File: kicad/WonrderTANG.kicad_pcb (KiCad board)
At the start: 2 copper layers, 101.6 x 90.2 mm, 31 parts, among them CON1 MSX-CONNECTOR, J1 Conn_02x01, J2 AudioJack3, J3 Conn_02x01, Q1 2N3904, U1 SN74LVC245AN, U2 SN74LVC245AN, U3 SN74LVC245AN, U4 SN74LVC245AN, U5 Tang_Nano_20k, U6 SN74LVC245AN

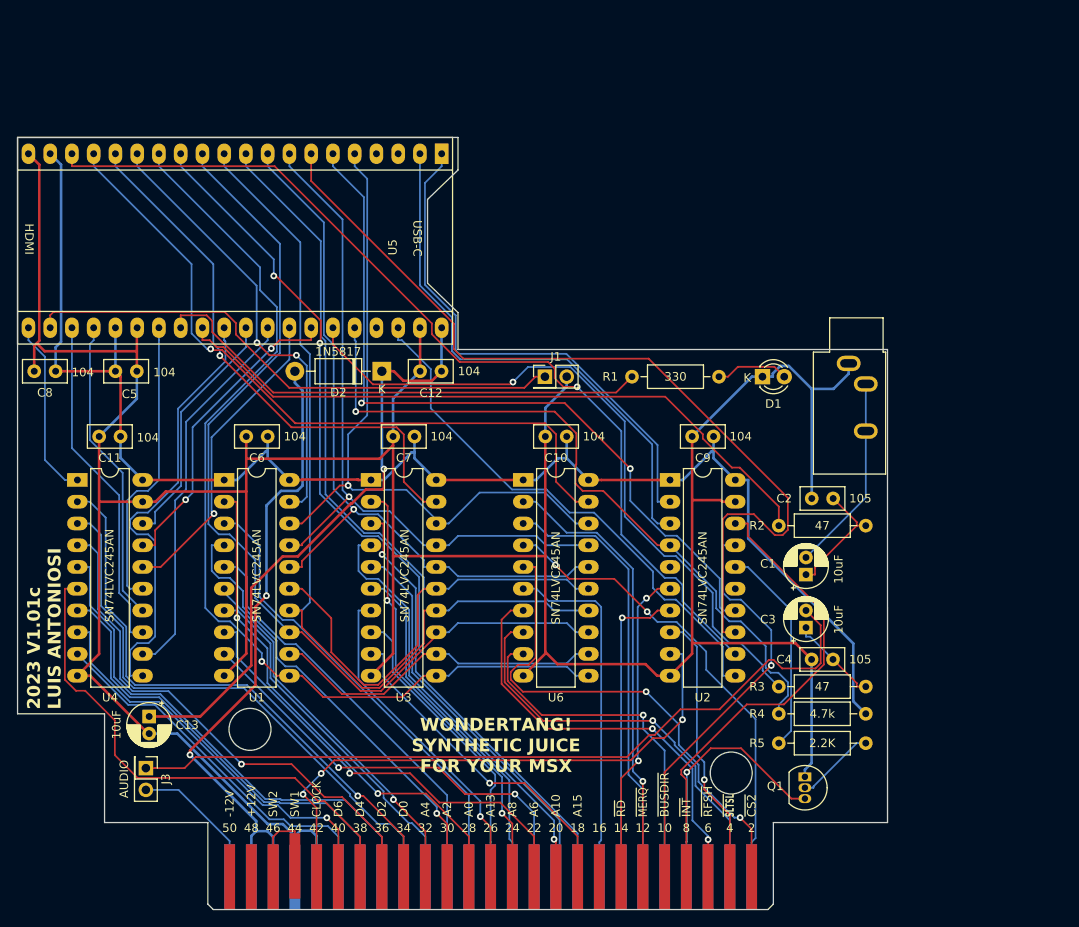
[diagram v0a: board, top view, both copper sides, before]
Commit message: New PCB Version 1.0.2d
A new firmware inverting the INT outpult needs to be submitted.
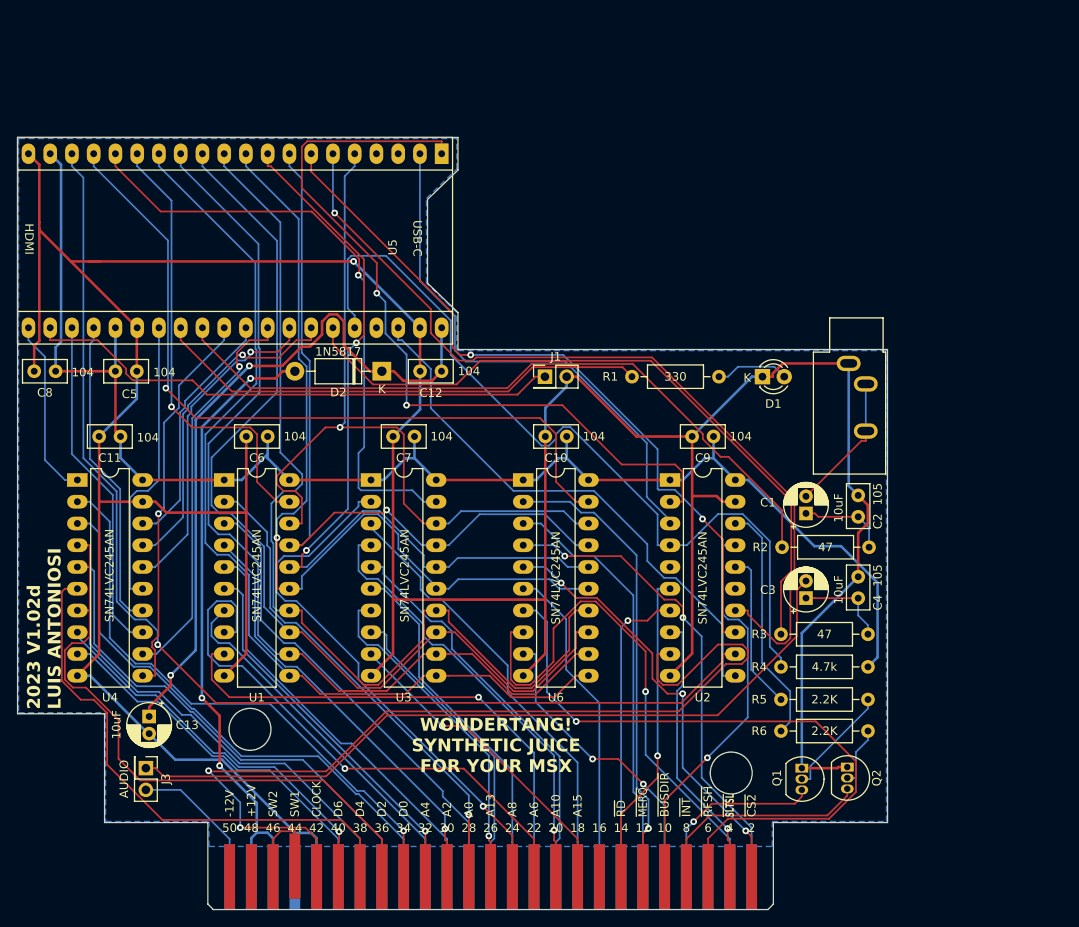
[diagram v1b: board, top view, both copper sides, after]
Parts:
- added Q2: 2N3904, Package_TO_SOT_THT:TO-92_Inline, F.Cu at (153.4, 126.9)
- added R6: 2.2K, Resistor_THT:R_Axial_DIN0207_L6.3mm_D2.5mm_P10.16mm_Horizontal, F.Cu at (145.7, 122.7)
- moved C4 7.73 mm to (154.7, 107.1), turned to 90 degrees
- moved C1 7.14 mm to (148.6, 97.2)
- moved R3 6.12 mm to (145.7, 111.4)
- moved R4 5.49 mm to (155.8, 115.2)
- moved R5 5.11 mm to (145.7, 119.0)
- moved C2 3.62 mm to (154.7, 97.6), turned to 90 degrees
- moved C3 3.45 mm to (148.6, 107.1)
- moved R2 2.55 mm to (145.8, 101.2)
- moved Q1 1.08 mm to (148.1, 127.0)
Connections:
- U2 pad 18: INT -> /INT_SW
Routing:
- net GND: track 406.2 -> 451.9 mm, vias 0 -> 1
- net CLOCK: track 67.5 -> 109.0 mm, vias 3 -> 2
- net INT_33: track 61.5 -> 93.7 mm, vias 0 -> 2
- net INT: track 56.1 -> 26.1 mm
- net RFSH: track 50.3 -> 78.5 mm, vias 2 -> 1
- net /INT_SW: track 0.00 -> 28.2 mm
- net SLTSL_33: track 112.1 -> 135.4 mm
- net WR_33: track 103.4 -> 85.4 mm, vias 0 -> 2
- net CS12: track 48.8 -> 62.1 mm
- net RD_33: track 88.6 -> 101.4 mm, vias 2 -> 1
- net WAIT_33: track 83.7 -> 96.4 mm, vias 1 -> 0
- net A6: track 52.7 -> 65.1 mm
- net MP2_33: track 88.0 -> 99.6 mm, vias 1 -> 2
- net A8: track 51.6 -> 63.1 mm, vias 2 -> 1
- net +5V: track 70.5 -> 82.0 mm, vias 1 -> 2
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- added copper zone on B.Cu, net GND
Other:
- board text added: "2023 V1.02d LUIS ANTONIOSI"
- board text removed: "2023 V1.01c LUIS ANTONIOSI"

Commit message: version 2.0b
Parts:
- removed C3: 10uF, Capacitor_THT:CP_Radial_D5.0mm_P2.00mm
- removed C4: 105, Capacitor_THT:C_Disc_D5.0mm_W2.5mm_P2.50mm
- removed J1: Conn_02x01, Connector_PinHeader_2.54mm:PinHeader_2x01_P2.54mm_Vertical
- removed R2, R3: 47, Resistor_THT:R_Axial_DIN0207_L6.3mm_D2.5mm_P10.16mm_Horizontal
- C1: value 10uF -> 4.7u; footprint Capacitor_THT:CP_Radial_D5.0mm_P2.00mm -> Capacitor_THT:CP_Radial_D5.0mm_P2.50mm
- C2: value 105 -> 4.7u; footprint Capacitor_THT:C_Disc_D5.0mm_W2.5mm_P2.50mm -> Capacitor_THT:CP_Radial_D5.0mm_P2.50mm
- CON1: footprint Mis_huellas:CARTRIDGE_MSX -> Tang20K:CARTRIDGE_MSX_NOCUT
- D1: value LED -> uSD
- J2: footprint Connector_Audio:Jack_3.5mm_CUI_SJ1-3533NG_Horizontal -> Tang20K:SJ1-3523N
- J3: value Conn_02x01 -> AUDIO
- Q1, Q2: footprint Package_TO_SOT_THT:TO-92_Inline -> Package_TO_SOT_THT:TO-92_Inline_Wide
- U5: footprint Mis_huellas:Tang_Nano_20k -> Tang20K:Tang_Nano_20k_Audio
- moved J3 86.4 mm to (107.7, 48.5), turned to 0 degrees
- moved C13 70.5 mm to (116.8, 66.6)
- moved C1 58.2 mm to (92.2, 111.8), turned to 0 degrees
- moved Q1 34.3 mm to (170.8, 101.3)
- moved R4 34.1 mm to (176.3, 87.9)
- moved R5 33.3 mm to (166.1, 92.7)
- moved R6 32.4 mm to (166.1, 97.5)
- moved C9 25.2 mm to (158.8, 74.3)
- moved U6 25.2 mm to (136.6, 79.3)
- moved C11 25.2 mm to (89.5, 74.3)
- moved C6 25.2 mm to (106.7, 74.3)
- moved C7 25.2 mm to (123.9, 74.3)
- moved U1 25.2 mm to (101.6, 79.3)
- moved U3 25.2 mm to (118.8, 79.3)
- moved U4 25.2 mm to (84.5, 79.3)
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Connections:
- C1 pad 1: Net-(C1-Pad1) -> Net-(J3-Pin_1)
- C1 pad 2: Net-(C1-Pad2) -> SOUNDIN
- C2 pad 1: Net-(C1-Pad1) -> Net-(J3-Pin_2)
- C2 pad 2: GND -> Net-(C2-Pad2)
- J2 pad R: Net-(C1-Pad2) -> Net-(C2-Pad2)
- J2 pad T: Net-(C1-Pad2) -> Net-(C2-Pad2)
- J3 pad 2: SOUNDIN -> Net-(J3-Pin_2)
- U5 pad 22: JP -> D6_33
- U5 pad 28: LED -> D2_33
- U5 pad 29: SOUND_33 -> D7_33
- U5 pad 3: unconnected-(U5-75_IOT34A-Pad3) -> LED
- U5 pad 35: AUDIO_33 -> D1_33
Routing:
- net SOUND_33: track 84.4 -> 0.00 mm
- net AUDIO_33: track 81.4 -> 0.00 mm
- net Net-(J3-Pin_2): track 0.00 -> 78.3 mm, vias 0 -> 1
- net JP: track 63.1 -> 0.00 mm
- net +5V: track 82.0 -> 24.9 mm, vias 2 -> 0
- net GND: track 451.9 -> 412.2 mm
- net RFSH: track 78.5 -> 41.1 mm, vias 1 -> 2
- net CLOCK: track 109.0 -> 140.5 mm, vias 2 -> 0
- net SLTSL_33: track 135.4 -> 107.9 mm, vias 1 -> 0
- net CS1: track 56.5 -> 79.9 mm, vias 2 -> 0
- net CS12: track 62.1 -> 40.2 mm
- net A15: track 37.6 -> 58.9 mm, vias 1 -> 0
- net MP4_33: track 116.6 -> 95.8 mm
- net D4_33: track 36.6 -> 57.1 mm
- net LED: track 58.3 -> 38.1 mm
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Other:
- board size 101.6 x 90.2 mm -> 101.6 x 89.5 mm
- board text added: "2024 V2.0b LUIS ANTONIOSI"
- board text added: "SSLT0: uSD Drive + Nextor SSLT1: OPLL + FM ROM SSLT2: 2MB Megaram+SCC SSLT3: 4MB Memory Mapper SMS VDP/PSG (Franky HDMI)"
- board text removed: "2023 V1.02d LUIS ANTONIOSI"

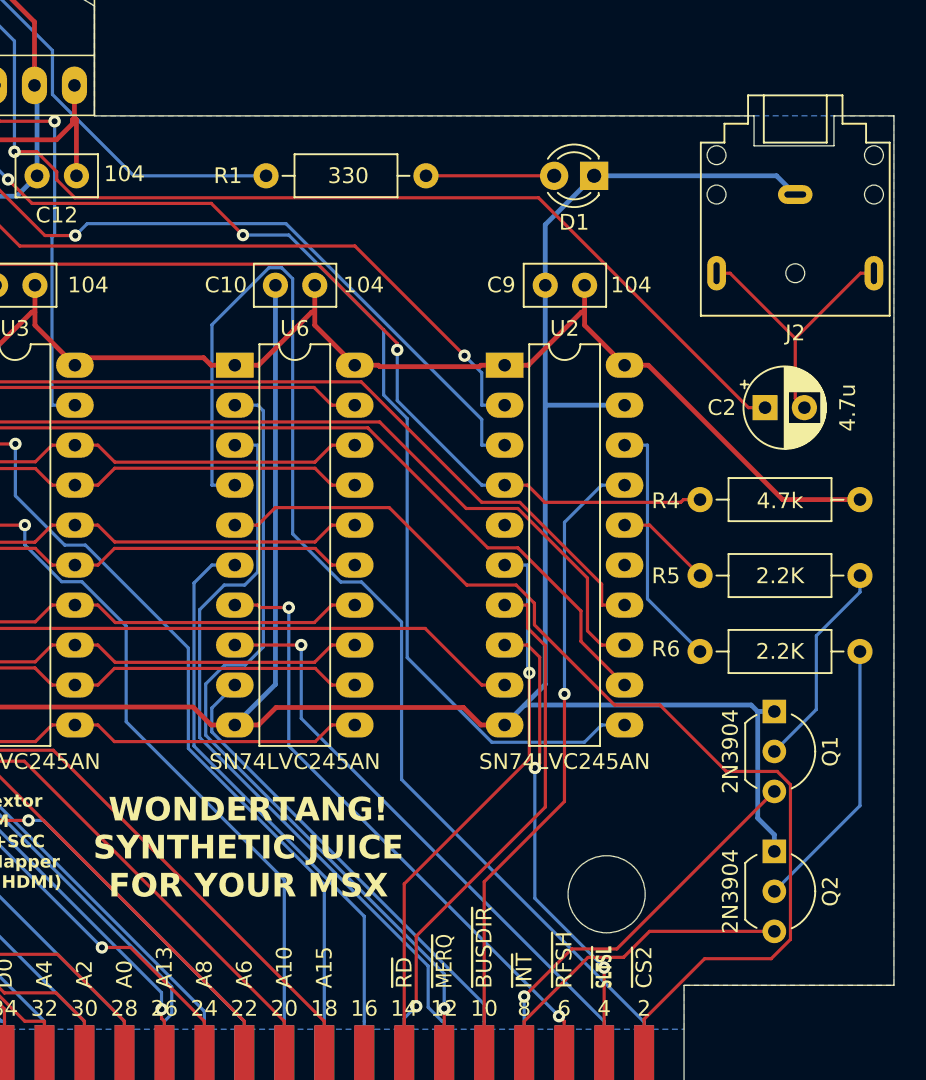
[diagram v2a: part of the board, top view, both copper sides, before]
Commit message: Changed pcb width to 99.965mm, reducing the pcbway fabrication cost fro 5 to , which is the standard cost to 5 protoboards. Only right side of the pcb was shifted left, no other changes were made
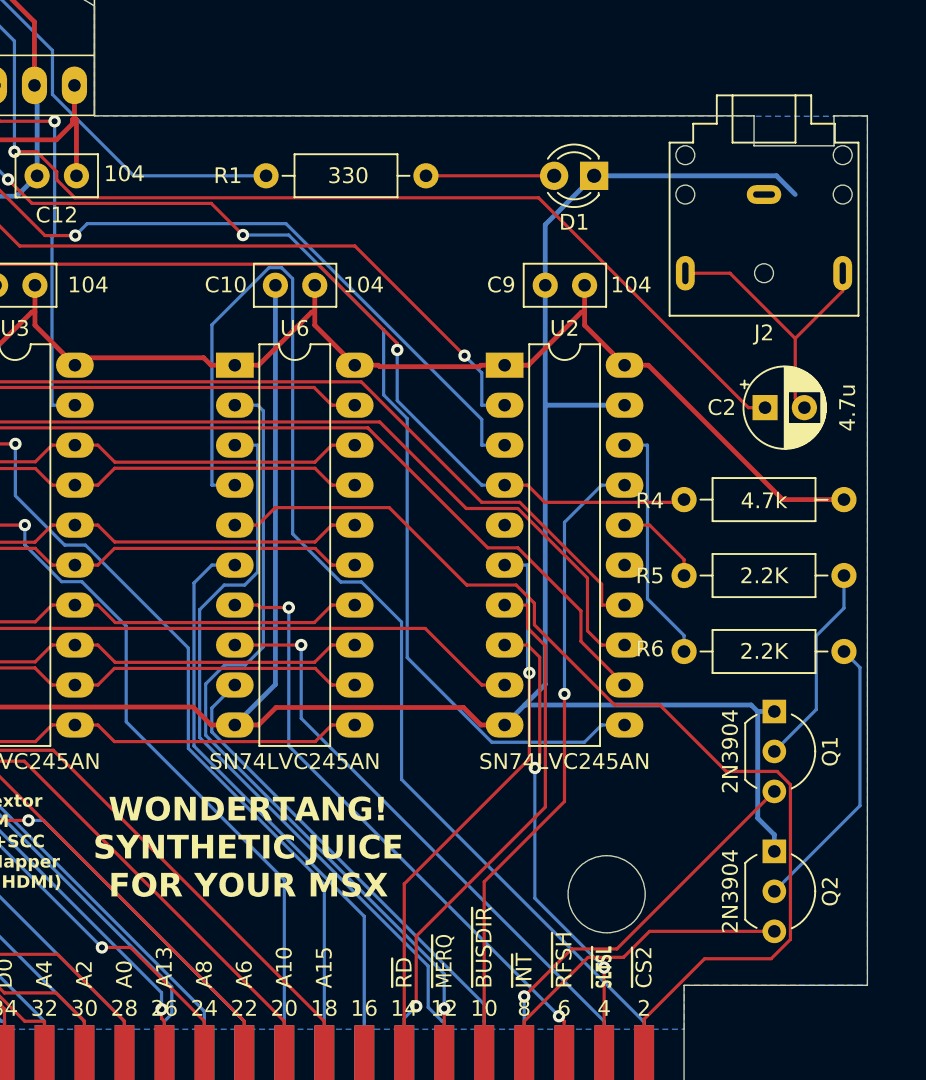
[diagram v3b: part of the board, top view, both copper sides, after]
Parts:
- moved J2 1.98 mm to (170.2, 68.5)
- moved R4 1.02 mm to (175.3, 87.9)
- moved R5 1.02 mm to (165.1, 92.7)
- moved R6 1.02 mm to (165.1, 97.5)
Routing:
- net WAIT_33: track 82.4 -> 81.3 mm
- net +3.3V: track 161.4 -> 160.3 mm
- net Net-(C2-Pad2): track 18.1 -> 18.7 mm
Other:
- board size 101.6 x 89.5 mm -> 99.9 x 89.5 mm
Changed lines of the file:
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@@
 	(footprint "Resistor_THT:R_Axial_DIN0207_L6.3mm_D2.5mm_P10.16mm_Horizontal"
 		(layer "F.Cu")
-		(at 166.116 92.71)
+		(at 165.1 92.71)
 		(descr "Resistor, Axial_DIN0207 series, Axial, Horizontal, pin pitch=10.16mm, 0.25W = 1/4W, length*diameter=6.3*2.5mm^2, http://cdn-reichelt.de/documents/datenblatt/B400/1_4W%23YAG.pdf")
 		(tags "Resistor Axial_DIN0207 series Axial Horizontal pin pitch 10.16mm 0.25W = 1/4W length 6.3mm diameter 2.5mm")
@@
 	(footprint "Tang20K:SJ1-3523N"
 		(layer "F.Cu")
-		(at 172.165 68.5 180)
+		(at 170.18 68.5 180)
 		(descr "TRS 3.5mm, horizontal, through-hole, https://www.cuidevices.com/product/resource/pdf/sj1-352xn.pdf")
 		(tags "TRS audio jack stereo horizontal")
@@
 	(footprint "Resistor_THT:R_Axial_DIN0207_L6.3mm_D2.5mm_P10.16mm_Horizontal"
 		(layer "F.Cu")
-		(at 176.276 87.884 180)
+		(at 175.26 87.884 180)
 		(descr "Resistor, Axial_DIN0207 series, Axial, Horizontal, pin pitch=10.16mm, 0.25W = 1/4W, length*diameter=6.3*2.5mm^2, http://cdn-reichelt.de/documents/datenblatt/B400/1_4W%23YAG.pdf")
 		(tags "Resistor Axial_DIN0207 series Axial Horizontal pin pitch 10.16mm 0.25W = 1/4W length 6.3mm diameter 2.5mm")
@@
 	(footprint "Resistor_THT:R_Axial_DIN0207_L6.3mm_D2.5mm_P10.16mm_Horizontal"
 		(layer "F.Cu")
-		(at 166.116 97.536)
+		(at 165.1 97.536)
 		(descr "Resistor, Axial_DIN0207 series, Axial, Horizontal, pin pitch=10.16mm, 0.25W = 1/4W, length*diameter=6.3*2.5mm^2, http://cdn-reichelt.de/documents/datenblatt/B400/1_4W%23YAG.pdf")
 		(tags "Resistor Axial_DIN0207 series Axial Horizontal pin pitch 10.16mm 0.25W = 1/4W length 6.3mm diameter 2.5mm")
@@
 	(gr_line
 		(start 165.1 118.745)
-		(end 178.435 118.745)
+		(end 176.75 118.745)
 		(stroke
 			(width 0.05)
@@
 	)
 	(gr_line
-		(start 178.435 63.5)
+		(start 176.75 63.5)
 		(end 174.625 63.5)
 		(stroke
@@
 	)
 	(gr_line
-		(start 178.435 118.745)
-		(end 178.435 63.5)
+		(start 176.75 118.745)
+		(end 176.75 63.5)
 		(stroke
 			(width 0.05)
@@
 	)
 	(segment
-		(start 161.32 79.345)
-		(end 162.8265 79.345)
-		(width 0.3048)
-		(layer "F.Cu")
-		(net 1)
-	)
-	(segment
 		(start 158.78 76.805)
 		(end 161.32 79.345)
@@
 	)
 	(segment
-		(start 171.3655 87.884)
-		(end 176.276 87.884)
-		(width 0.3048)
-		(layer "F.Cu")
-		(net 1)
-	)
-	(segment
 		(start 141.4334 75.9731)
 		(end 138.0615 79.345)
@@
 	)
 	(segment
+		(start 161.32 79.345)
+		(end 162.8265 79.345)
+		(width 0.3048)
+		(layer "F.Cu")
+		(net 1)
+	)
+	(segment
 		(start 145.6815 79.345)
 		(end 145.7751 79.4386)
@@
 	)
 	(segment
+		(start 171.3655 87.884)
+		(end 175.26 87.884)
+		(width 0.3048)
+		(layer "F.Cu")
+		(net 1)
+	)
+	(segment
 		(start 125.9216 78.8716)
 		(end 134.5751 78.8716)
@@
 	)
 	(segment
-		(start 116.205 61.565)
-		(end 116.205 63.0207)
+		(start 165.0603 87.884)
+		(end 164.8848 88.0595)
 		(width 0.2032)
 		(layer "F.Cu")
@@
 	)
 	(segment
-		(start 141.8409 72.9256)
-		(end 146.8759 77.9606)
+		(start 116.205 61.565)
+		(end 116.205 63.0207)
 		(width 0.2032)
 		(layer "F.Cu")
@@
 	)
 	(segment
-		(start 156.2502 88.0595)
-		(end 164.8848 88.0595)
+		(start 141.8409 72.9256)
+		(end 146.8759 77.9606)
 		(width 0.2032)
 		(layer "F.Cu")
@@
 	)
 	(segment
-		(start 166.116 87.884)
-		(end 165.0603 87.884)
+		(start 155.1557 86.965)
+		(end 153.7 86.965)
 		(width 0.2032)
 		(layer "F.Cu")
@@
 	)
 	(segment
-		(start 111.1261 63.0207)
-		(end 107.6993 66.4475)
+		(start 156.2502 88.0595)
+		(end 155.1557 86.965)
 		(width 0.2032)
 		(layer "F.Cu")
@@
 	)
 	(segment
-		(start 155.1557 86.965)
-		(end 156.2502 88.0595)
+		(start 111.1261 63.0207)
+		(end 107.6993 66.4475)
 		(width 0.2032)
 		(layer "F.Cu")
@@
 	)
 	(segment
-		(start 107.8719 69.0525)
-		(end 113.6437 69.0525)
+		(start 164.8848 88.0595)
+		(end 156.2502 88.0595)
 		(width 0.2032)
 		(layer "F.Cu")
@@
 	)
 	(segment
-		(start 164.8848 88.0595)
-		(end 165.0603 87.884)
+		(start 107.8719 69.0525)
+		(end 113.6437 69.0525)
 		(width 0.2032)
 		(layer "F.Cu")
@@
 		(net 73)
 	)
-	(segment
-		(start 153.7 86.965)
-		(end 155.1557 86.965)
-		(width 0.2032)
-		(layer "F.Cu")
-		(net 73)
-	)
 	(via
 		(at 146.8759 78.373)
@@
 	)
 	(segment
-		(start 177.165 73.5)
-		(end 176.3093 73.5)
+		(start 168.0207 73.5)
+		(end 172.165 77.6443)
 		(width 0.2032)
 		(layer "F.Cu")
@@
 	)
 	(segment
-		(start 176.3093 73.5)
+		(start 175.18 74.6293)
 		(end 172.165 77.6443)
 		(width 0.2032)
@@
 	)
 	(segment
-		(start 167.165 73.5)
+		(start 165.18 73.5)
 		(end 168.0207 73.5)
 		(width 0.2032)
@@
 	)
 	(segment
-		(start 168.0207 73.5)
-		(end 172.165 77.6443)
+		(start 175.18 73.5)
+		(end 175.18 74.6293)
 		(width 0.2032)
 		(layer "F.Cu")
@@
 	)
 	(segment
-		(start 170.836 103.886)
-		(end 173.5029 101.2191)
+		(start 175.26 94.7817)
+		(end 173.5029 96.5388)
 		(width 0.2032)
 		(layer "B.Cu")
@@
 	)
 	(segment
-		(start 173.5029 101.2191)
-		(end 173.5029 96.5388)
+		(start 175.26 92.71)
+		(end 175.26 94.7817)
 		(width 0.2032)
 		(layer "B.Cu")
@@
 	)
 	(segment
-		(start 176.276 92.71)
-		(end 176.276 93.7657)
+		(start 173.5029 96.5388)
+		(end 173.5029 101.2191)
 		(width 0.2032)
 		(layer "B.Cu")
@@
 	)
 	(segment
-		(start 173.5029 96.5388)
-		(end 176.276 93.7657)
+		(start 173.5029 101.2191)
+		(end 170.836 103.886)
 		(width 0.2032)
 		(layer "B.Cu")
@@
 	)
 	(segment
-		(start 166.116 92.71)
+		(start 162.911 89.505)
+		(end 161.32 89.505)
+		(width 0.2032)
+		(layer "F.Cu")
+		(net 86)
+	)
+	(segment
+		(start 165.1 91.694)
 		(end 162.911 89.505)
 		(width 0.2032)
@@
 	)
 	(segment
-		(start 162.911 89.505)
-		(end 161.32 89.505)
+		(start 165.1 92.71)
+		(end 165.1 91.694)
 		(width 0.2032)
 		(layer "F.Cu")
@@
 	)
 	(segment
-		(start 176.276 107.336)
-		(end 176.276 97.536)
+		(start 176.276 98.552)
+		(end 175.26 97.536)
 		(width 0.2032)
 		(layer "B.Cu")
@@
 	)
 	(segment
-		(start 162.7757 94.1957)
-		(end 162.7757 84.425)
+		(start 176.276 107.336)
+		(end 176.276 98.552)
+		(width 0.2032)
+		(layer "B.Cu")
+		(net 88)
+	)
+	(segment
+		(start 162.7757 84.425)
+		(end 161.32 84.425)
 		(width 0.2032)
 		(layer "B.Cu")
@@
 	)
 	(segment
-		(start 166.116 97.536)
-		(end 162.7757 94.1957)
+		(start 165.1 97.536)
+		(end 165.1 96.52)
 		(width 0.2032)
 		(layer "B.Cu")
@@
 	)
 	(segment
-		(start 161.32 84.425)
+		(start 162.7757 94.1957)
 		(end 162.7757 84.425)
 		(width 0.2032)
@@
 		(net 89)
 	)
+	(segment
+		(start 165.1 96.52)
+		(end 162.7757 94.1957)
+		(width 0.2032)
+		(layer "B.Cu")
+		(net 89)
+	)
 	(zone
 		(net 2)
@@
 			(pts
 				(xy 76.835 39.37) (xy 76.835 106.045) (xy 86.995 106.045) (xy 86.995 118.745) (xy 99.06 118.745)
-				(xy 99.06 121.539) (xy 165.1 121.539) (xy 165.1 118.745) (xy 178.435 118.745) (xy 178.435 63.5)
+				(xy 99.06 121.539) (xy 165.1 121.539) (xy 165.1 118.745) (xy 176.738662 118.718598) (xy 176.741922 63.532603)
 				(xy 127.635 63.5) (xy 127.635 56.515) (xy 124.46 54.61) (xy 124.46 48.26) (xy 127.635 46.355) (xy 127.635 39.37)
 			)
